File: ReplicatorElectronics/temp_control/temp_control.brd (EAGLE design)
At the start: 44.5 x 42.2 mm, 12 parts, among them J1 SBH11-PBPC-D05-ST-BK, J2 OSTVN04A150, Q1 IRL640A, T1 MMBT2222A, T2 MMBT2222A, T3 MMBT3906LT1

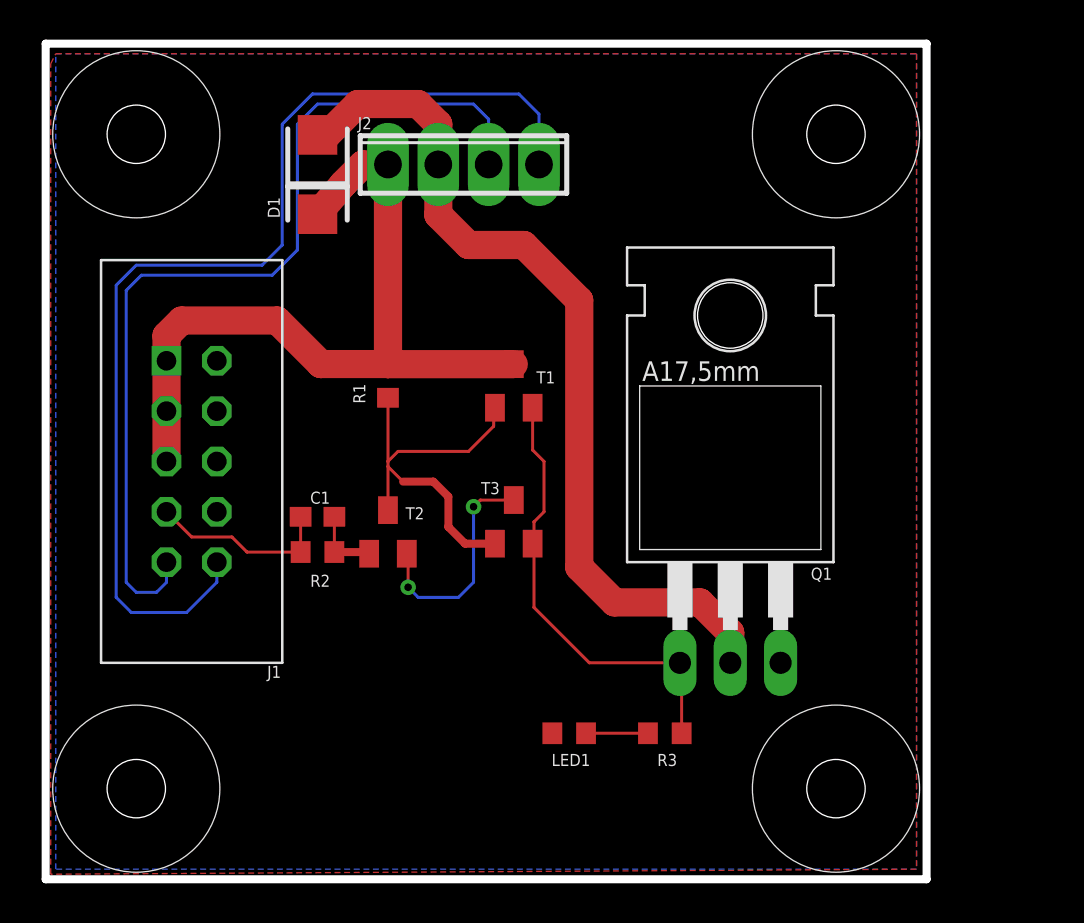
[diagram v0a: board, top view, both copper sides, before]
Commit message: 6/12/12: Added linearization circuit for potential thermocouple use. Can be DNP if not used.
~ 2 hrs.
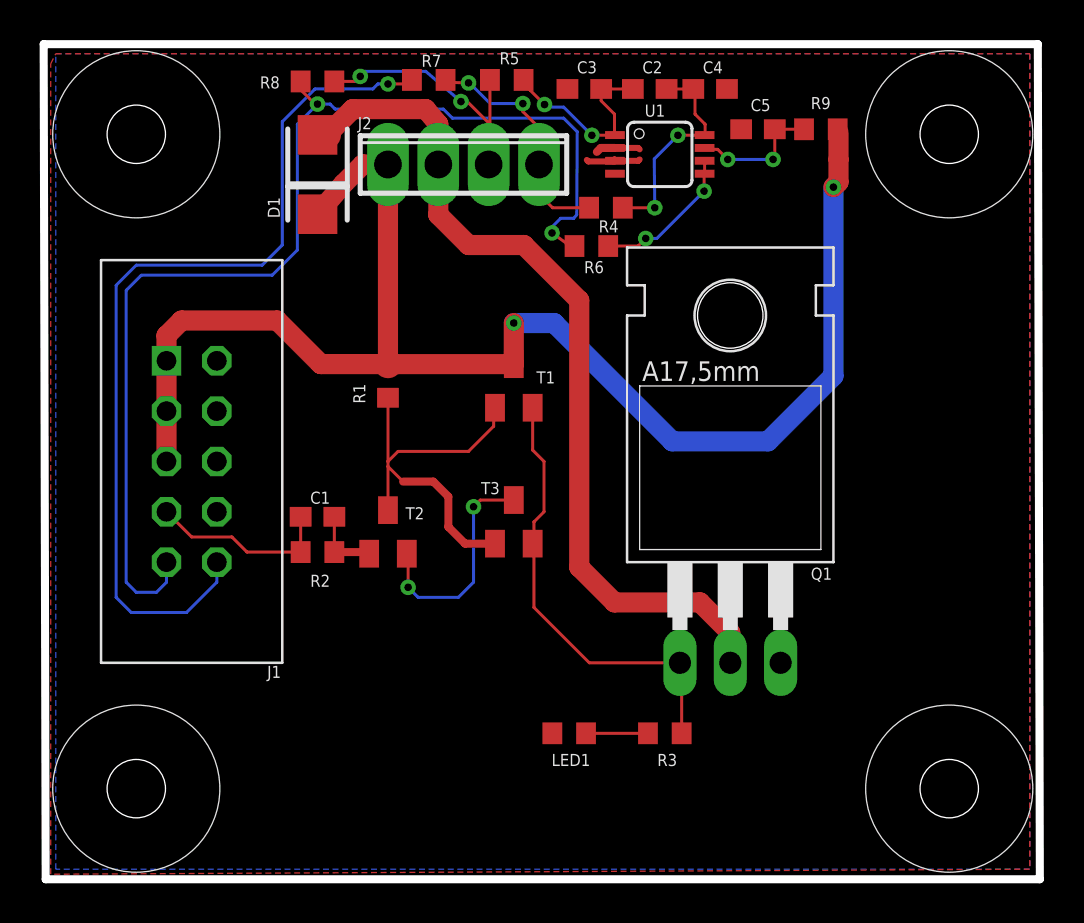
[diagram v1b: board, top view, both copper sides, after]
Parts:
- added C2: 10uF, resistor:C0603
- added C3, C4: 1uF, resistor:C0603
- added C5: 0.1uF, resistor:C0603
- added R4, R5: 10k, resistor:R0603
- added R6, R7, R8: 0, resistor:R0603
- added R9: 10, resistor:R0603
- added U1: AD8495, analog-devices:MSOP08
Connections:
- new net N$12: R6.1, U1.5, U1.6
- new net N$2: C2.2, C3.1, R5.1, U1.1
- new net N$5: C2.1, C4.2, R4.1, U1.8
- new net N$7: C5.1, R9.1, U1.7
- new net OUT1: J2.3, R5.2, R8.1
- new net OUT2: J2.4, R4.2, R7.1
- net GND: now also C3.2, C4.1, C5.2, U1.2, U1.3
- net THERM1: now also R6.2, R8.2; no longer J2.3
- net THERM2: now also R7.2; no longer J2.4
- net VCC: now also R9.2
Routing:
- net VCC: track 39.8 -> 74.4 mm, vias 0 -> 2
- net OUT1: track 0.00 -> 13.4 mm, vias 0 -> 2
- net OUT2: track 0.00 -> 12.1 mm, vias 0 -> 2
- net THERM1: track 46.7 -> 58.5 mm, vias 0 -> 2
- net N$5: track 0.00 -> 11.1 mm, vias 0 -> 2
- net N$2: track 0.00 -> 10.1 mm, vias 0 -> 2
- net THERM2: track 54.7 -> 45.6 mm, vias 0 -> 1
- net N$12: track 0.00 -> 7.53 mm, vias 0 -> 2
- net N$7: track 0.00 -> 6.73 mm, vias 0 -> 2
- net GND: track 0.00 -> 5.14 mm
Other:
- board size 44.5 x 42.2 mm -> 50.3 x 42.1 mm
